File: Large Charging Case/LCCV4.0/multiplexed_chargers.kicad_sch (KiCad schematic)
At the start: 26 parts, among them U17 74HC4051PW, U18 XL2902-TS, U19 74HCT259PW, U20 XL2902-TS

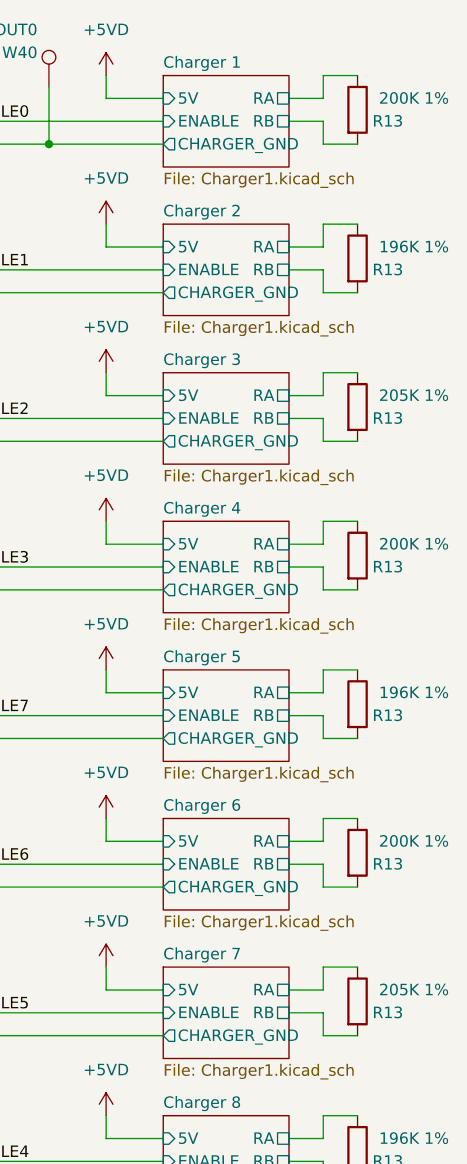
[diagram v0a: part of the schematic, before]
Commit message: Super6, LCCV4 updates and Kicad8
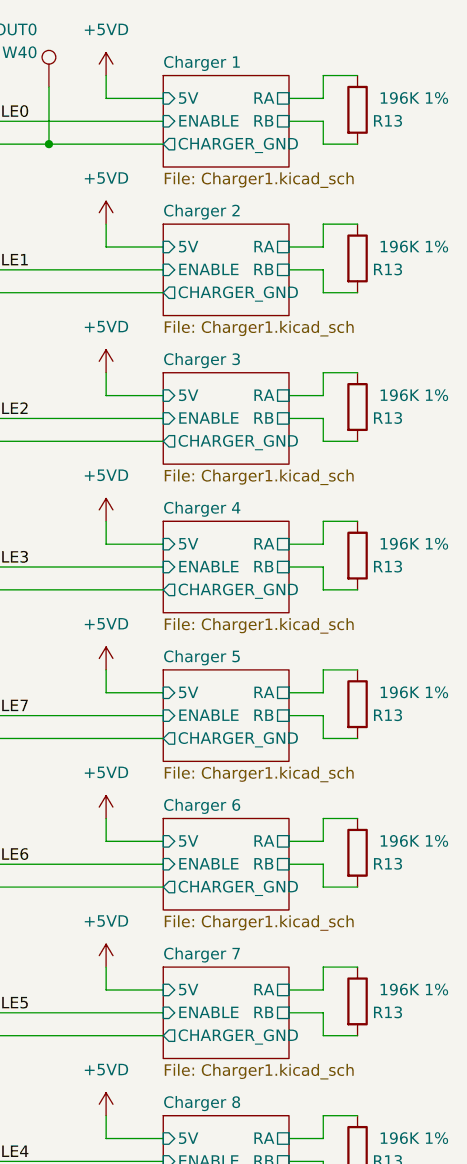
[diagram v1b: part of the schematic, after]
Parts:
- R13: value 205K 1% -> 196K 1%; Manufacturer Part Number 0402WGF2053TCE -> 0402WGF1963TCE
- R13: value 200K 1% -> 196K 1%; LCSC Part Number C25764 -> (none); Manufacturer Part Number 0402WGF2003TCE -> 0402WGF1963TCE
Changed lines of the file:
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@@
       (effects (font (size 1.27 1.27)) (justify right))
     )
-    (property "Value" "205K 1%" (at 274.32 54.61 0)
+    (property "Value" "196K 1%" (at 274.32 54.61 0)
       (effects (font (size 1.27 1.27)) (justify right))
     )
@@
       (effects (font (size 1.27 1.27)) hide)
     )
-    (property "Manufacturer Part Number" "0402WGF2053TCE" (at 264.16 55.88 0)
+    (property "Manufacturer Part Number" "0402WGF1963TCE" (at 264.16 55.88 0)
       (effects (font (size 1.27 1.27)) hide)
     )
@@
       (effects (font (size 1.27 1.27)) (justify right))
     )
-    (property "Value" "200K 1%" (at 274.32 21.59 0)
+    (property "Value" "196K 1%" (at 274.32 21.59 0)
       (effects (font (size 1.27 1.27)) (justify right))
     )
@@
       (effects (font (size 1.27 1.27)) hide)
     )
-    (property "LCSC Part Number" "C25764" (at 264.16 22.86 0)
+    (property "LCSC Part Number" "" (at 264.16 22.86 0)
       (effects (font (size 1.27 1.27)) hide)
     )
@@
       (effects (font (size 1.27 1.27)) hide)
     )
-    (property "Manufacturer Part Number" "0402WGF2003TCE" (at 264.16 22.86 0)
+    (property "Manufacturer Part Number" "0402WGF1963TCE" (at 264.16 22.86 0)
       (effects (font (size 1.27 1.27)) hide)
     )
@@
       (effects (font (size 1.27 1.27)) (justify right))
     )
-    (property "Value" "200K 1%" (at 274.32 71.12 0)
+    (property "Value" "196K 1%" (at 274.32 71.12 0)
       (effects (font (size 1.27 1.27)) (justify right))
     )
@@
       (effects (font (size 1.27 1.27)) hide)
     )
-    (property "LCSC Part Number" "C25764" (at 264.16 72.39 0)
+    (property "LCSC Part Number" "" (at 264.16 72.39 0)
       (effects (font (size 1.27 1.27)) hide)
     )
@@
       (effects (font (size 1.27 1.27)) hide)
     )
-    (property "Manufacturer Part Number" "0402WGF2003TCE" (at 264.16 72.39 0)
+    (property "Manufacturer Part Number" "0402WGF1963TCE" (at 264.16 72.39 0)
       (effects (font (size 1.27 1.27)) hide)
     )
@@
       (effects (font (size 1.27 1.27)) (justify right))
     )
-    (property "Value" "200K 1%" (at 274.32 104.14 0)
+    (property "Value" "196K 1%" (at 274.32 104.14 0)
       (effects (font (size 1.27 1.27)) (justify right))
     )
@@
       (effects (font (size 1.27 1.27)) hide)
     )
-    (property "LCSC Part Number" "C25764" (at 264.16 105.41 0)
+    (property "LCSC Part Number" "" (at 264.16 105.41 0)
       (effects (font (size 1.27 1.27)) hide)
     )
@@
       (effects (font (size 1.27 1.27)) hide)
     )
-    (property "Manufacturer Part Number" "0402WGF2003TCE" (at 264.16 105.41 0)
+    (property "Manufacturer Part Number" "0402WGF1963TCE" (at 264.16 105.41 0)
       (effects (font (size 1.27 1.27)) hide)
     )
@@
       (effects (font (size 1.27 1.27)) (justify right))
     )
-    (property "Value" "205K 1%" (at 274.32 120.65 0)
+    (property "Value" "196K 1%" (at 274.32 120.65 0)
       (effects (font (size 1.27 1.27)) (justify right))
     )
@@
       (effects (font (size 1.27 1.27)) hide)
     )
-    (property "Manufacturer Part Number" "0402WGF2053TCE" (at 264.16 121.92 0)
-      (effects (font (size 1.27 1.27)) hide)
-    )
+    (property "Manufacturer Part Number" "0402WGF1963TCE" (at 264.16 121.92 0)
+      (effects (font (size 1.27 1.27)) hide)
+    )

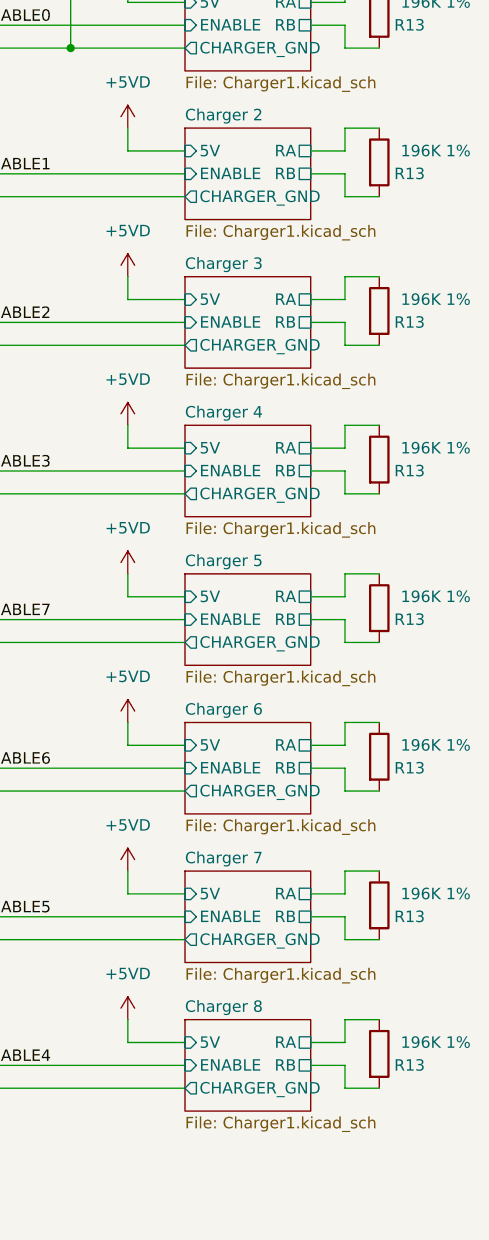
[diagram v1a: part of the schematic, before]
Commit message: Updated a bunch of boards, added Jogs and 12mm D6 proto
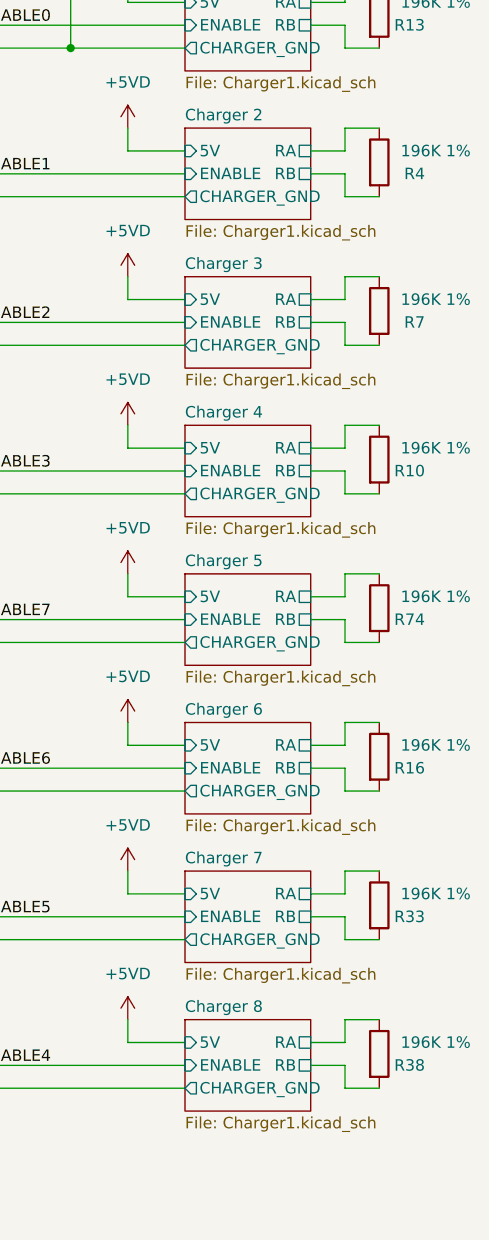
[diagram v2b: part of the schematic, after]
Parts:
- renumbered R13 to R10, R13 to R16, R13 to R33, R13 to R38, R13 to R4, R13 to R7, R13 to R74
